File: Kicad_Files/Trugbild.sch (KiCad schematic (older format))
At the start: 90 parts, among them J1 Conn_02x05_Odd_Even, J2 HDMI_A, J3 Conn_01x02, J4 HDMI_A, U1 AS4C32M8SA-6TIN, U2 XC3S50A-4VQG100C, U3 MIC5365-3.3YD5, U4 LDK130PU12R_DFN6, U5 MX25L1636EM2I-08G, X1 EC5645ETTS-50.000M

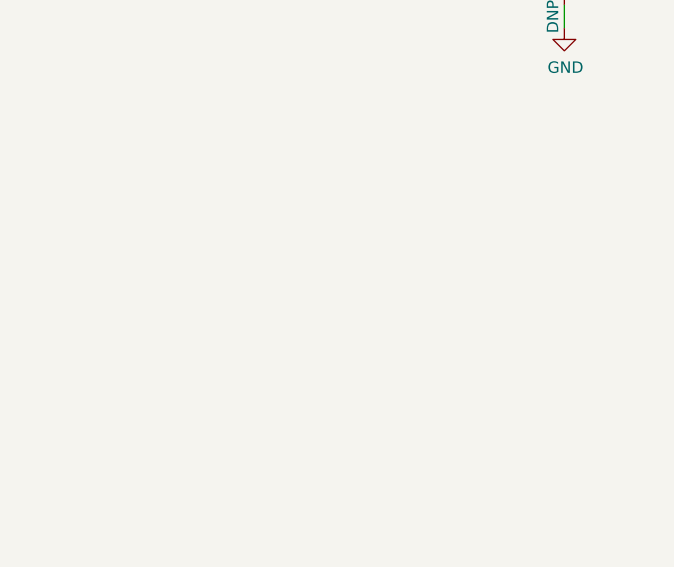
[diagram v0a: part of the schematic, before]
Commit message: fix for JLCPCB clearance
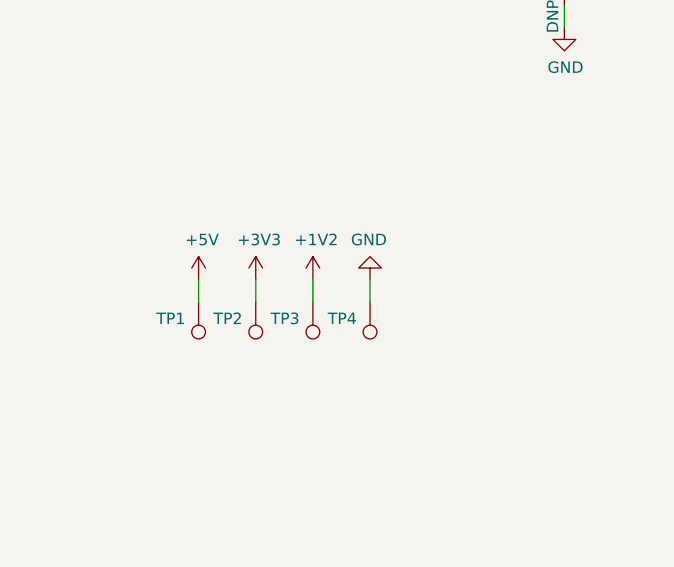
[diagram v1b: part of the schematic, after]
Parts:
- added TP1, TP2, TP3, TP4: TestPoint, TestPoint:TestPoint_Pad_D1.0mm, symbol Connector:TestPoint
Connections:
- wire segments 404 -> 408
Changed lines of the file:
@@
 encoding utf-8
 Sheet 1 1
-Title ""
-Date ""
-Rev ""
-Comp ""
-Comment1 ""
-Comment2 ""
+Title "Trugbild"
+Date "2021-07-15"
+Rev "1.0"
+Comp "Jakub Kajzer"
+Comment1 "jakubkajzer@gmail.com"
+Comment2 "You can contact me by email:"
 Comment3 ""
 Comment4 ""
@@
 	1    0    0    -1
 $EndComp
-Wire Wire Line
-	6050 1100 6500 1100
 $Comp
 L Device:C C24
@@
 Wire Wire Line
 	8550 1200 8550 1100
-Wire Wire Line
-	9250 1100 9700 1100
 $Comp
 L Device:C C28
@@
 Wire Wire Line
 	6150 10500 6750 10500
+$Comp
+L Connector:TestPoint TP1
+U 1 1 61017825
+P 1300 4450
+F 0 "TP1" H 1358 4522 50  0000 L CNN
+F 1 "TestPoint" H 1358 4477 50  0001 L CNN
+F 2 "TestPoint:TestPoint_Pad_D1.0mm" H 1500 4450 50  0001 C CNN
+F 3 "~" H 1500 4450 50  0001 C CNN
+	1    1300 4450
+	-1   0    0    1
+$EndComp
+Wire Wire Line
+	9250 1100 9700 1100
+Wire Wire Line
+	6050 1100 6500 1100
+$Comp
+L Connector:TestPoint TP2
+U 1 1 6107D254
+P 1550 4450
+F 0 "TP2" H 1608 4522 50  0000 L CNN
+F 1 "TestPoint" H 1608 4477 50  0001 L CNN
+F 2 "TestPoint:TestPoint_Pad_D1.0mm" H 1750 4450 50  0001 C CNN
+F 3 "~" H 1750 4450 50  0001 C CNN
+	1    1550 4450
+	-1   0    0    1
+$EndComp
+$Comp
+L Connector:TestPoint TP3
+U 1 1 6107D5E6
+P 1800 4450
+F 0 "TP3" H 1858 4522 50  0000 L CNN
+F 1 "TestPoint" H 1858 4477 50  0001 L CNN
+F 2 "TestPoint:TestPoint_Pad_D1.0mm" H 2000 4450 50  0001 C CNN
+F 3 "~" H 2000 4450 50  0001 C CNN
+	1    1800 4450
+	-1   0    0    1
+$EndComp
+$Comp
+L Connector:TestPoint TP4
+U 1 1 6107D966
+P 2050 4450
+F 0 "TP4" H 2108 4522 50  0000 L CNN
+F 1 "TestPoint" H 2108 4477 50  0001 L CNN
+F 2 "TestPoint:TestPoint_Pad_D1.0mm" H 2250 4450 50  0001 C CNN
+F 3 "~" H 2250 4450 50  0001 C CNN
+	1    2050 4450
+	-1   0    0    1
+$EndComp
+$Comp
+L power:GND #PWR025
+U 1 1 6107DD7A
+P 2050 4350
+F 0 "#PWR025" H 2050 4100 50  0001 C CNN
+F 1 "GND" H 2055 4177 50  0000 C CNN
+F 2 "" H 2050 4350 50  0001 C CNN
+F 3 "" H 2050 4350 50  0001 C CNN
+	1    2050 4350
+	-1   0    0    1
+$EndComp
+$Comp
+L power:+5V #PWR022
+U 1 1 6107E8C3
+P 1300 4350
+F 0 "#PWR022" H 1300 4200 50  0001 C CNN
+F 1 "+5V" H 1315 4523 50  0000 C CNN
+F 2 "" H 1300 4350 50  0001 C CNN
+F 3 "" H 1300 4350 50  0001 C CNN
+	1    1300 4350
+	1    0    0    -1
+$EndComp
+$Comp
+L power:+3V3 #PWR023
+U 1 1 61080050
+P 1550 4350
+F 0 "#PWR023" H 1550 4200 50  0001 C CNN
+F 1 "+3V3" H 1565 4523 50  0000 C CNN
+F 2 "" H 1550 4350 50  0001 C CNN
+F 3 "" H 1550 4350 50  0001 C CNN
+	1    1550 4350
+	1    0    0    -1
+$EndComp
+$Comp
+L power:+1V2 #PWR024
+U 1 1 61080B6C
+P 1800 4350
+F 0 "#PWR024" H 1800 4200 50  0001 C CNN
+F 1 "+1V2" H 1815 4523 50  0000 C CNN
+F 2 "" H 1800 4350 50  0001 C CNN
+F 3 "" H 1800 4350 50  0001 C CNN
+	1    1800 4350
+	1    0    0    -1
+$EndComp
+Wire Wire Line
+	1300 4450 1300 4350
+Wire Wire Line
+	1550 4450 1550 4350
+Wire Wire Line
+	1800 4350 1800 4450
+Wire Wire Line
+	2050 4350 2050 4450
 $EndSCHEMATC
